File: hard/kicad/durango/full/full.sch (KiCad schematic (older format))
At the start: 40 parts, among them J1 NANOLINK, J2 IOX8, J3 IOX9, J4 BUZZER, Q1 BC547, Q2 BC547, Q3 BC547, SW1 RESET, U1 65C02, U104 74HC257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

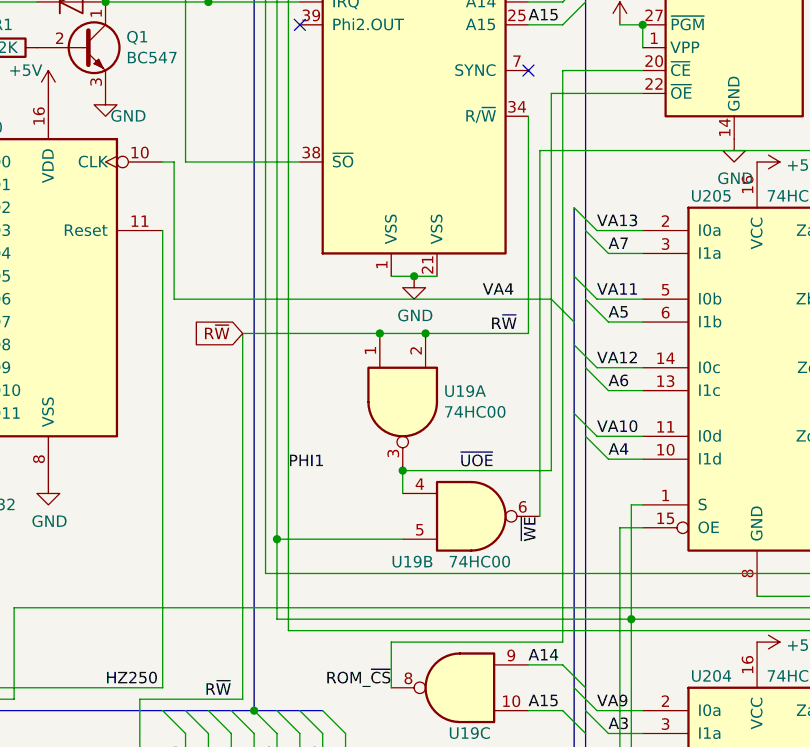
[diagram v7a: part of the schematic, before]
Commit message: fixed DeMorgan HIRES enabled output
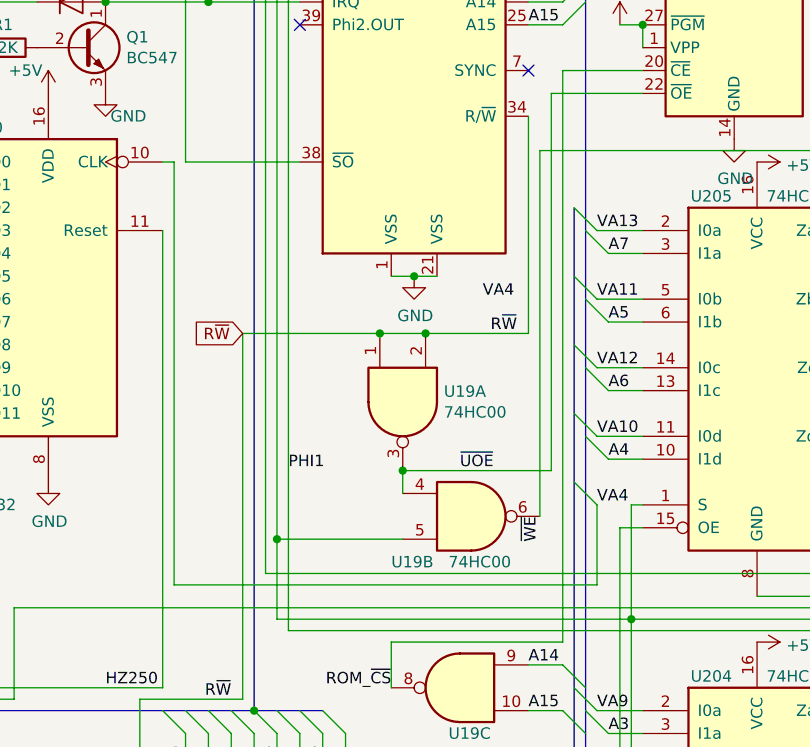
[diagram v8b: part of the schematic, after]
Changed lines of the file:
@@
 EESchema Schematic File Version 4
 LIBS:full-cache
-EELAYER 30 0
+EELAYER 29 0
 EELAYER END
 $Descr A4 11693 8268
@@
 Wire Wire Line
 	2900 2050 2900 4800
-Entry Wire Line
-	4100 3750 4200 3850
-Wire Wire Line
-	4100 3750 2450 3750
 Text Label 3800 3750 0    50   ~ 0
 VA4
 Wire Wire Line
-	2450 3150 2450 3750
-Wire Wire Line
 	2450 3150 2400 3150
+Entry Wire Line
+	4200 4550 4300 4650
+Wire Wire Line
+	4300 4650 4300 5000
+Wire Wire Line
+	4300 5000 2450 5000
+Wire Wire Line
+	4100 2850 4100 4500
+Wire Wire Line
+	2450 3150 2450 5000
 Wire Wire Line
 	10600 1050 10850 1050
@@
 Wire Bus Line
 	4250 700  4250 7300
-Wire Wire Line
-	4100 2850 4100 4500
+Text Label 4300 4650 0    50   ~ 0
+VA4
 $EndSCHEMATC
